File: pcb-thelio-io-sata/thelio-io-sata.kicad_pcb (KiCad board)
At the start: 4 copper layers, 72 x 50 mm, 14 parts

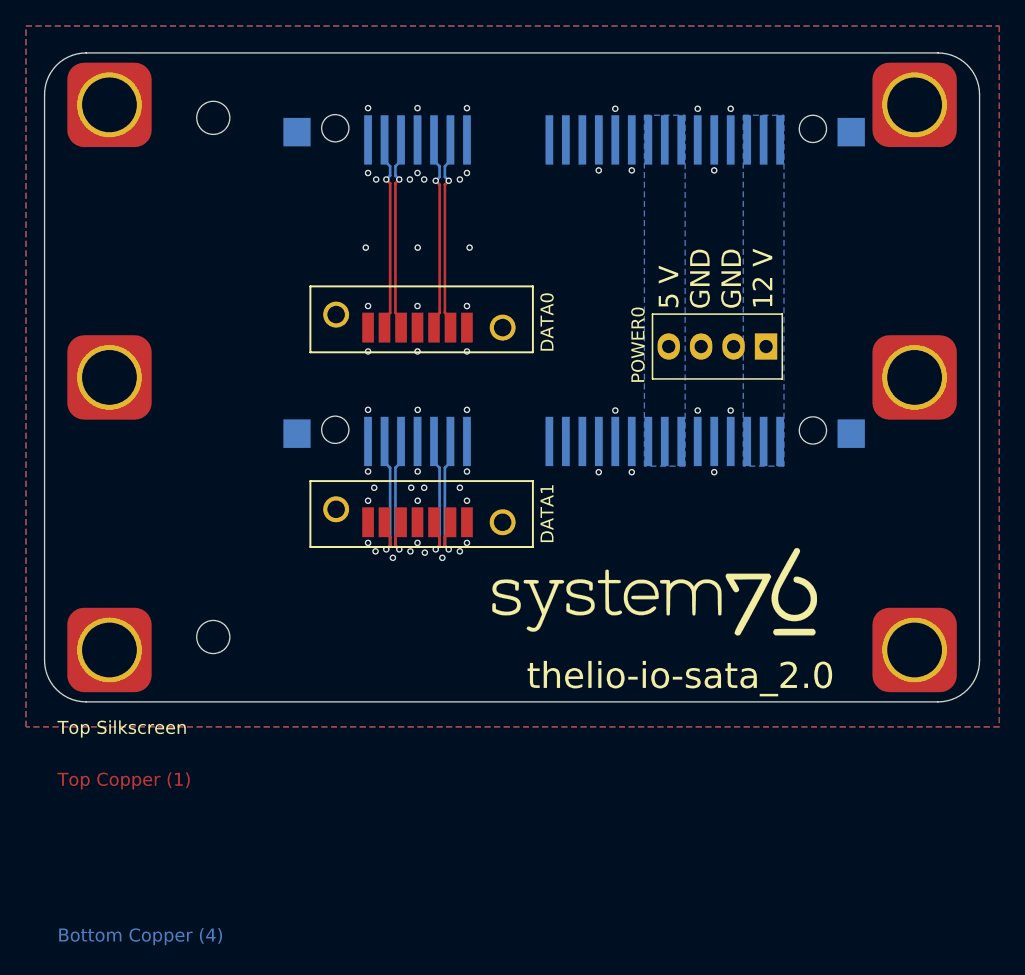
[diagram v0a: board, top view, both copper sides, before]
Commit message: thelio-io-sata 2.2 shrink board outline reduce number of mounting standoffs use PEM part number
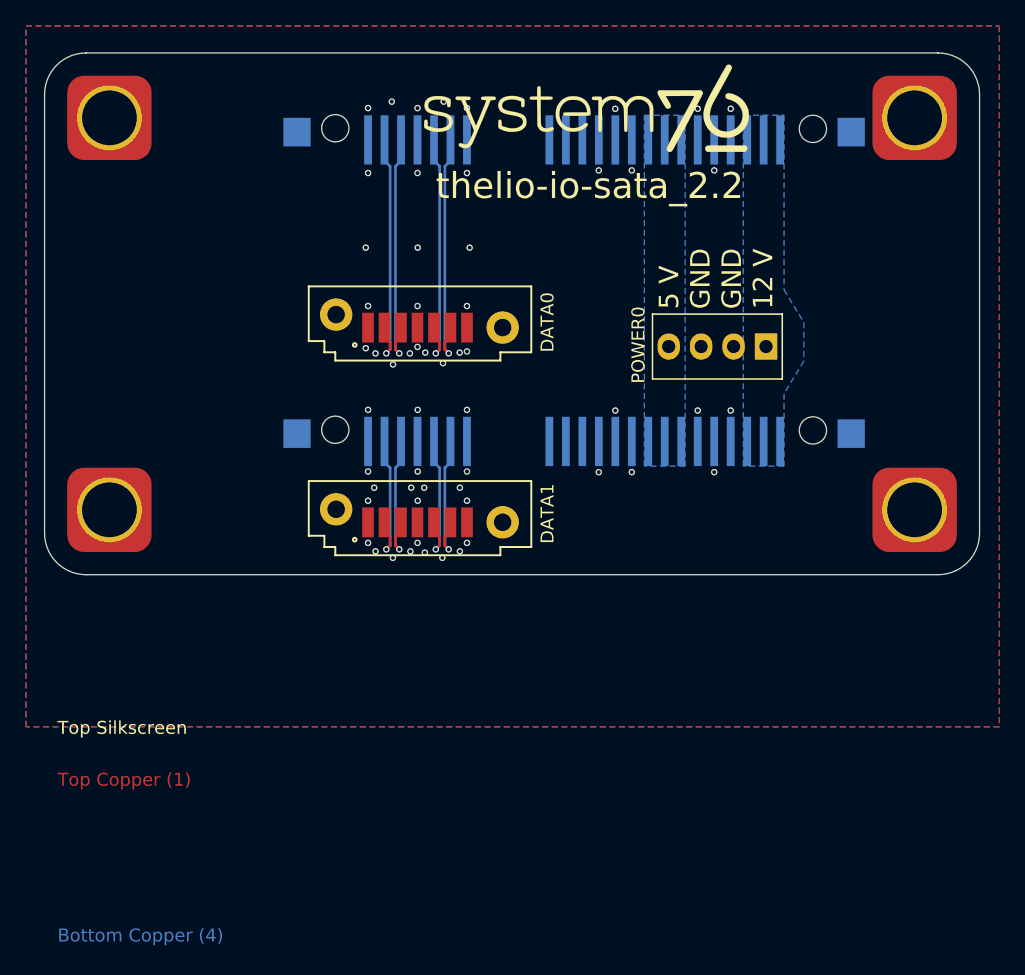
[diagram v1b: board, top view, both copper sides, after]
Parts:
- removed H5, H6: SMTSOM330STR, SMTSO:SMTSO-M3-3
- removed TH? (x2): th, kicad_pcb:tooling_hole_2.55
- H1, H2, H3, H4: value SMTSOM330STR -> SMTSO-M3-3ET
- moved G*** 37.6 mm to (68.8, 54.2)
- moved H3 10.2 mm to (32.0, 85.2)
- moved H4 10.2 mm to (94.0, 85.2)
- moved H1 1.00 mm to (32.0, 55.0)
- moved H2 1.00 mm to (94.0, 55.0)
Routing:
- net /SATA0_A+: track 15.1 -> 18.3 mm
- net /SATA0_B+: track 15.1 -> 18.3 mm
- net /SATA0_A-: track 15.1 -> 18.3 mm
- net /SATA0_B-: track 15.1 -> 18.3 mm
- net GND: vias 53 -> 57
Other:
- board size 72 x 50 mm -> 72 x 40.2 mm
- rule pad_to_mask_clearance: 0.2 -> 0.075
- rule solder_mask_min_width: 0.25 -> 0.1
- board text added: "thelio-io-sata_2.2"
- board text added: "thelio-io-sata_2.2 Board must be RoHS compliant Fabricate to IPC-A-600 Class II Material: Shengyi S1000-2 or equivalent Inner copper 1 or 1/2 oz Outer copper, min 33.4 um finished Black LPI solder mask over bare copper Vendor may remove solder mask from via holes, maximum of drill size + 3 mil Finish: OSP Silkscreen: white non conductive 100% electrical test required Remove all unused pads from i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"
- board text removed: "thelio-io-sata_2.0"
- board text removed: "thelio-io-sata_2.0 Board must be RoHS compliant Fabricate to IPC-A-600 Class II Material: Shengyi S1000-2 or equivalent Inner copper 1 or 1/2 oz Outer copper, min 33.4 um finished Black LPI solder mask over bare copper Vendor may remove solder mask from via holes, maximum of drill size + 3 mil Finish: OSP Silkscreen: white non conductive 100% electrical test required Remove all unused pads from i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"
